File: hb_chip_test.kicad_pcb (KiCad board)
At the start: 2 copper layers, 140 parts, among them J1 31-5431-2010_CID2.5.196, J2 31-5431-2010_CID2.5.196, J3 31-5431-2010_CID2.5.196, J4 1945193_12P_CID2.2.928, J5 31-5431-2010_CID2.5.196, J6 31-5431-2010_CID2.5.196, U1 L7812ABD2T-TR_CID8.52.934, U2 MC7912ACD2TR4G_CID8.52.429, U3 LP2981IM5-5.0-NOPB_CID8.52.176, U5 TL084, U6 MCP3202, U7 REF5050ID

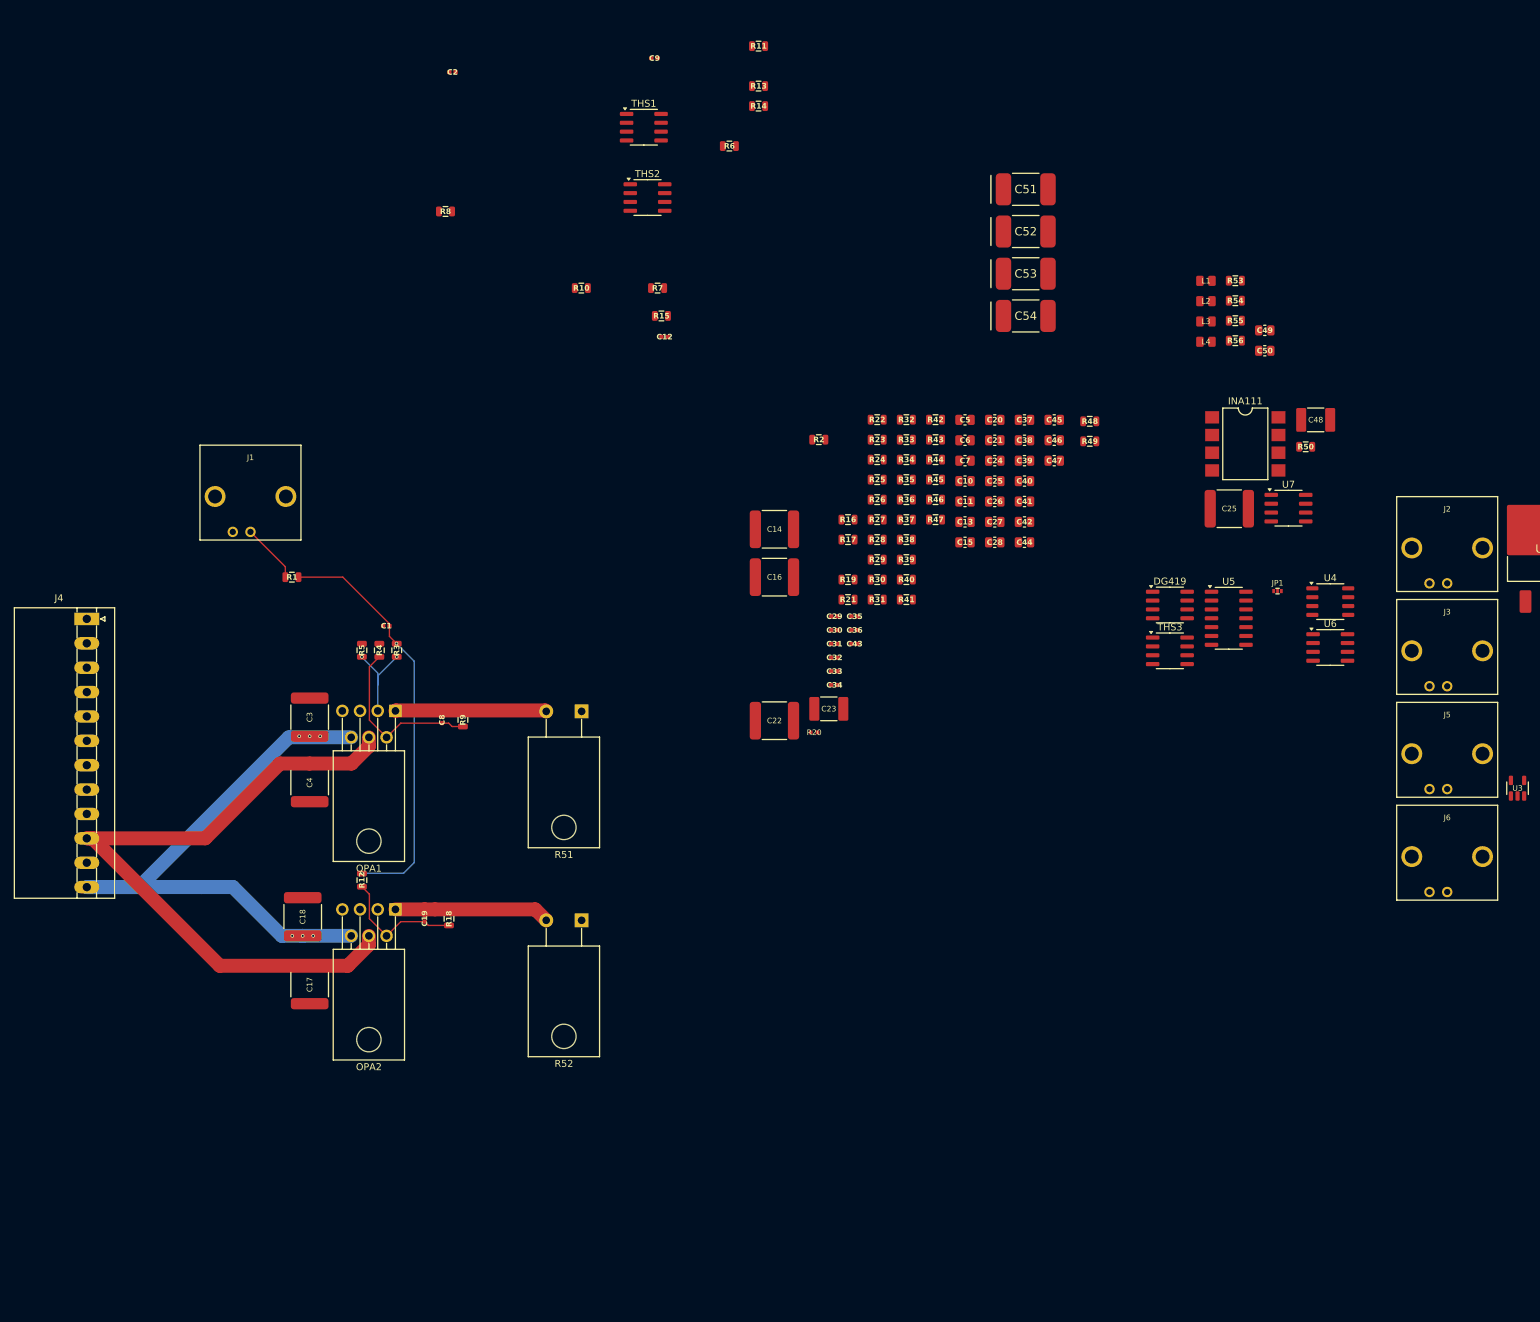
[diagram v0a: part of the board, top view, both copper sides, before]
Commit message: Variable amps and offset circuit
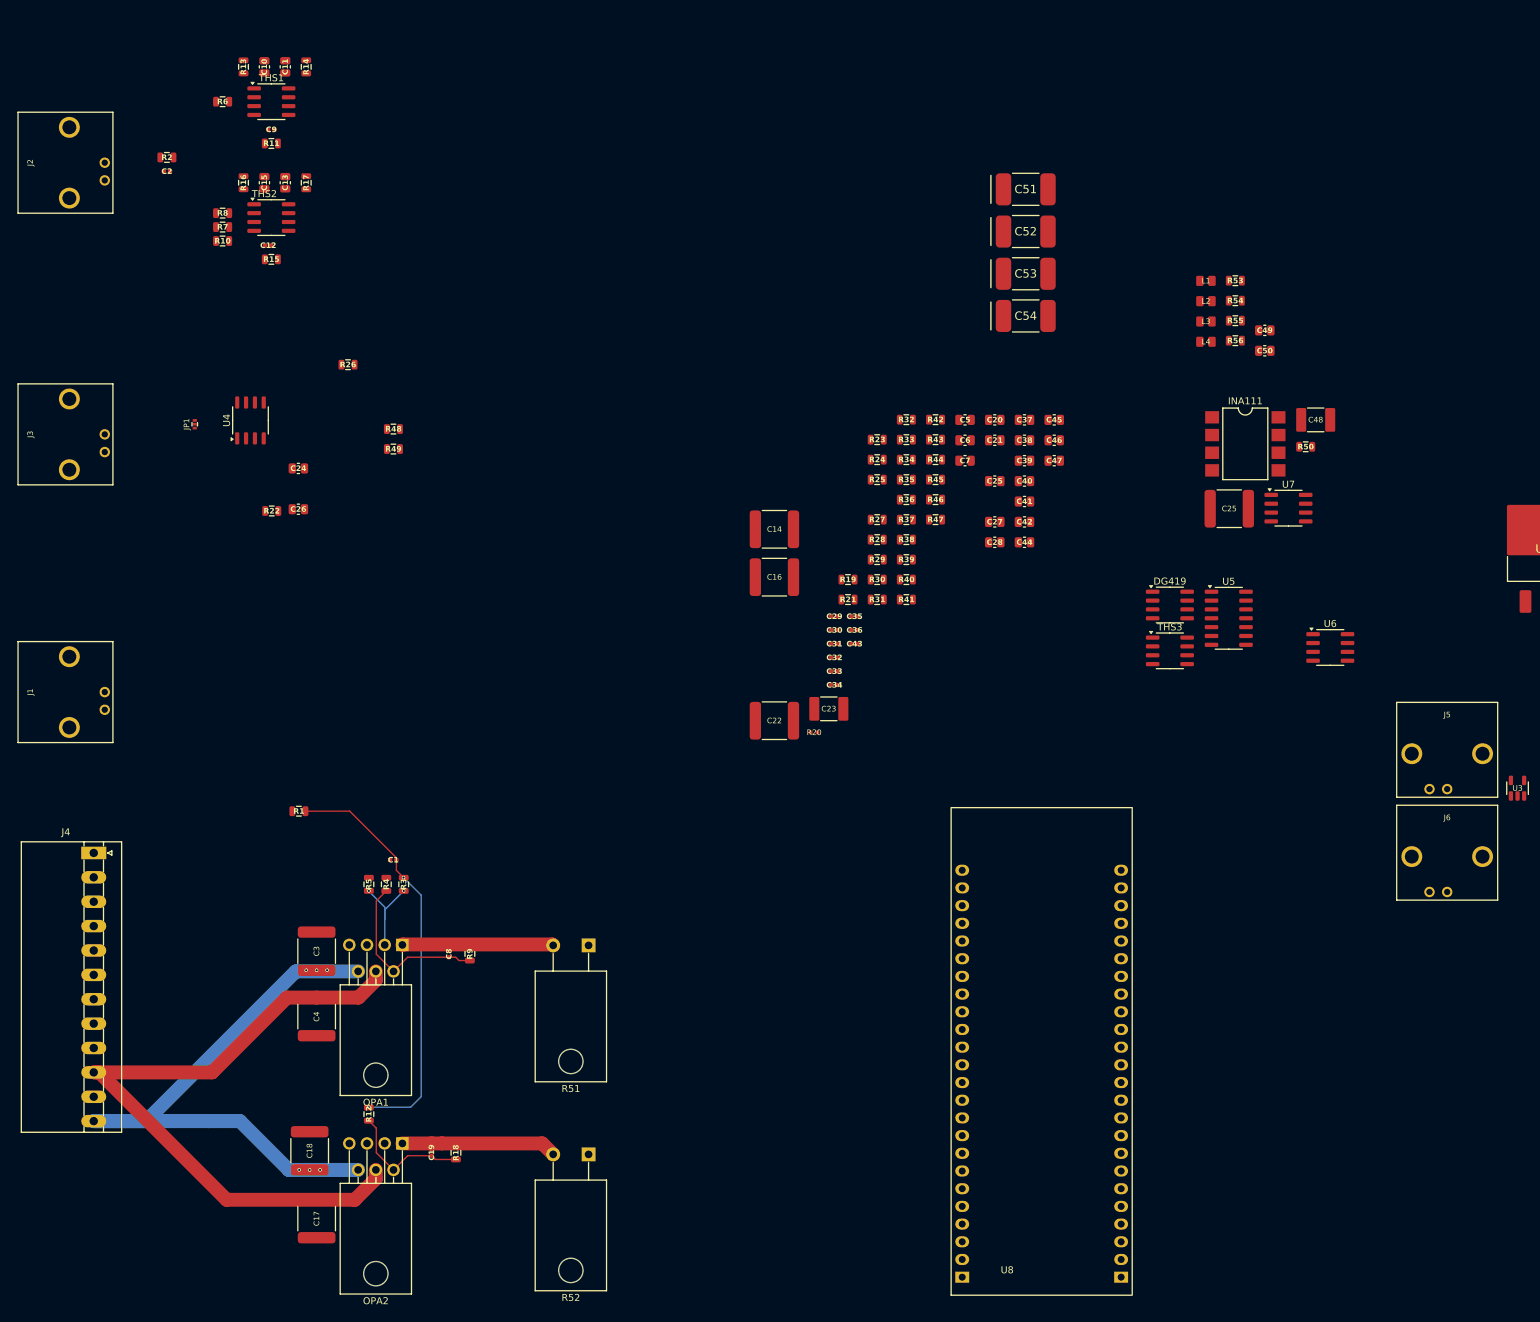
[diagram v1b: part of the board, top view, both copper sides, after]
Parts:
- added U8: Tang_Nano_9K, 0my_project:DIP-48_TangNano9K, F.Cu at (160.6, 163.8)
- moved J2 205.4 mm to (21.0, 33.0), turned to 90 degrees
- moved J3 200.2 mm to (21.0, 72.0), turned to 90 degrees
- moved JP1 157.3 mm to (39.0, 70.5), turned to 90 degrees
- moved U4 157.2 mm to (47.0, 70.0), turned to 90 degrees
- moved C10 116.9 mm to (49.0, 19.2), turned to 90 degrees
- moved C11 115.8 mm to (52.0, 19.2), turned to 90 degrees
- moved C15 113.1 mm to (49.0, 35.9), turned to 90 degrees
- moved C13 109.1 mm to (52.0, 35.9), turned to 90 degrees
- moved R2 102.0 mm to (35.0, 32.2)
- moved C24 100.0 mm to (53.9, 76.9)
- moved C26 100.0 mm to (53.9, 82.8)
- moved R48 100.0 mm to (67.5, 71.2)
- moved R49 100.0 mm to (67.5, 74.1)
- moved R16 99.4 mm to (46.0, 35.9), turned to 90 degrees
- moved R17 93.1 mm to (55.0, 35.9), turned to -90 degrees
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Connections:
- R8 pad 1: unconnected-(R8-Pad1) -> GND
- R8 pad 2: unconnected-(R8-Pad2) -> Net-(THS2--)
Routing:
- net Net-(J1-Pad1): track 8.57 -> 0.00 mm

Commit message: HB driver jumpers + PCBv1
TangNano9k has been wired.

Jumpers place for the hb drive but no bnc's for this. If something else is to drive it it can be done from jumpers.

PCB is in the layout v1 now. Still missing socket for the chip.
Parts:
- removed the C25 at (153.9, 78.7)
- added C55: C_0805_100nF_16V_X7R_CID1.2.3078, dtuspace_ipc:C0805_CAPC200X125X130L45N, F.Cu at (211.3, 60.2)
- added C56: C_0805_100nF_16V_X7R_CID1.2.3078, dtuspace_ipc:C0805_CAPC200X125X130L45N, F.Cu at (219.0, 68.3)
- added C57: C_0402_3.3nF_16V_X7R_CID1.2.2599, dtuspace_ipc:C0402_CAPC100X50X61L25N, F.Cu at (112.4, 66.3)
- added C58: C_2917_47uF_20V_20%_CID1.3.892, dtuspace_ipc:C2917_CAPC730X430X310L130N, F.Cu at (101.3, 157.0)
- added C59: C_2917_47uF_20V_20%_CID1.3.892, dtuspace_ipc:C2917_CAPC730X430X310L130N, F.Cu at (112.0, 157.0)
- added C60: C_2917_47uF_20V_20%_CID1.3.892, dtuspace_ipc:C2917_CAPC730X430X310L130N, F.Cu at (129.8, 157.0)
- added C61: C_2917_47uF_20V_20%_CID1.3.892, dtuspace_ipc:C2917_CAPC730X430X310L130N, F.Cu at (141.0, 157.0)
- added D1: CUS520,H3F_CID4.2.447, dtuspace_ipc:SOD250X130X120L30X30N, F.Cu at (235.5, 108.0)
- added D2: CUS520,H3F_CID4.2.447, dtuspace_ipc:SOD250X130X120L30X30N, F.Cu at (235.5, 104.0)
- added J13: 2x8, dtuspace_ipc:HEADER-P254-2x8, F.Cu at (225.5, 120.0)
- added J7: 31-5431-2010_CID2.5.196, dtuspace_ipc:AMPHENOL_31-5431-2010, F.Cu at (240.9, 65.8)
- added J8: 2x8, dtuspace_ipc:HEADER-P254-2x8, F.Cu at (212.8, 154.8)
- added JP2: Jumper_3_Open, dtuspace_ipc:HEADER-P254-1x3, F.Cu at (178.9, 33.1)
- added JP3: Jumper_3_Open, dtuspace_ipc:HEADER-P254-1x3, F.Cu at (214.0, 72.3)
- added JP4: Jumper_3_Open, dtuspace_ipc:HEADER-P254-1x3, F.Cu at (187.9, 51.1)
- added JP5: Jumper_3_Open, dtuspace_ipc:HEADER-P254-1x3, F.Cu at (114.5, 48.9)
- added JP6: Jumper_3_Open, dtuspace_ipc:HEADER-P254-1x3, F.Cu at (114.4, 35.2)
- added L5: L_3.3uH_870mA_CID7.3.944, dtuspace_ipc:L0805_INDC200X125X140L50N, F.Cu at (104.7, 162.5)
- added L6: L_3.3uH_870mA_CID7.3.944, dtuspace_ipc:L0805_INDC200X125X140L50N, F.Cu at (108.7, 162.5)
- added L7: L_3.3uH_870mA_CID7.3.944, dtuspace_ipc:L0805_INDC200X125X140L50N, F.Cu at (133.0, 161.0)
- added L8: L_3.3uH_870mA_CID7.3.944, dtuspace_ipc:L0805_INDC200X125X140L50N, F.Cu at (137.5, 163.5)
- added R57: R_0805_51R1_CID10.9.208, dtuspace_ipc:R0805_RESC200X125X50L35N, F.Cu at (176.4, 29.6)
- added R58: R_0805_511k_CID10.9.489, dtuspace_ipc:R0805_RESC200X125X50L35N, F.Cu at (217.4, 57.4)
- added R59: R_0805_511k_CID10.9.489, dtuspace_ipc:R0805_RESC200X125X50L35N, F.Cu at (215.4, 57.4)
- added R60: R_0805_511k_CID10.9.489, dtuspace_ipc:R0805_RESC200X125X50L35N, F.Cu at (214.9, 68.2)
- added R61: R_0805_1M21_CID10.9.5950, dtuspace_ipc:R0805_RESC200X125X50L35N, F.Cu at (212.9, 68.3)
- added R62: R_0805_10R0_CID10.9.4757, dtuspace_ipc:R0805_RESC200X125X50L35N, F.Cu at (211.3, 58.2)
- added R63: R_0805_51k1_CID10.9.5890, dtuspace_ipc:R0805_RESC200X125X50L35N, F.Cu at (208.9, 68.3)
- added R64: R_0805_5k11_CID10.9.467, dtuspace_ipc:R0805_RESC200X125X50L35N, F.Cu at (210.9, 68.3)
- added R65: R_0805_10R0_CID10.9.4757, dtuspace_ipc:R0805_RESC200X125X50L35N, F.Cu at (217.0, 68.2)
- added R66: R_0805_9k53_CID10.9.5867, dtuspace_ipc:R0805_RESC200X125X50L35N, F.Cu at (227.4, 113.5)
- added R67: R_0805_5k11_CID10.9.467, dtuspace_ipc:R0805_RESC200X125X50L35N, F.Cu at (229.4, 113.5)
- added R68: R_0805_1K_CID10.99.611, dtuspace_ipc:R0805_RESC200X125X50L35N, F.Cu at (111.9, 64.8)
- added U9: TL082, dtuspace_ipc:SOIC8P127_490X600X175L83X41N, F.Cu at (215.8, 62.7)
- C39, C46, C47: value C_0805_100nF_16V_X7R_CID1.2.3078 -> C_0402_22nF_16V_X7R_CID1.2.2613; footprint dtuspace_ipc:C0805_CAPC200X125X130L45N -> dtuspace_ipc:C0402_CAPC100X50X61L25N
- JP1: footprint dtuspace_ipc:2_WAY_SOLDER_JUMPER -> dtuspace_ipc:HEADER-P254-1x3
- R35, R46: value R_0805_11k0_CID10.9.5869 -> R_0805_26k1_CID10.9.5881
- R38, R41, R43, R45: value R_0805_11k0_CID10.9.5869 -> R_0805_11k5_CID10.9.5870
- R40, R44: value R_0805_5k62_CID10.9.159 -> R_0805_11k5_CID10.9.5870
- R47: value R_0805_5k62_CID10.9.159 -> R_0805_26k1_CID10.9.5881
- R53: value R_0805_220R_CID10.9.602 -> R_0805_1K_CID10.99.611
- R55: value R_0805_2M49_CID10.9.5964 -> R_0805_2k49_CID10.9.5859
- R56: value R_0805_10M0_CID10.9.5993 -> R_0805_10k0_CID10.9.476
- moved LD_SML-P11VTT86R2 223.8 mm to (71.0, 138.5), turned to 90 degrees
- moved LD_SML-P11VTT86R3 213.9 mm to (71.0, 118.0), turned to 180 degrees
- moved LD_SML-P11VTT86R1 211.4 mm to (71.0, 107.9), turned to 90 degrees
- moved U2 173.8 mm to (74.8, 127.6), turned to 180 degrees
- moved U1 168.4 mm to (74.8, 148.6), turned to 180 degrees
- moved U3 155.7 mm to (73.9, 107.9), turned to 90 degrees
- moved LD_SML-P11VTT86R4 143.9 mm to (164.2, 134.8), turned to 90 degrees
- moved L3 130.4 mm to (90.0, 146.0), turned to 90 degrees
- moved C53 124.5 mm to (83.5, 148.5), turned to -90 degrees
- moved L4 117.7 mm to (90.4, 129.8), turned to -90 degrees
- moved C20 114.7 mm to (68.0, 146.0), turned to -90 degrees
- moved L2 113.1 mm to (85.9, 108.9), turned to 180 degrees
- moved C43 112.5 mm to (225.5, 37.0), turned to 90 degrees
- moved C51 109.4 mm to (171.0, 145.5)
- moved C54 104.1 mm to (83.4, 127.3), turned to -90 degrees
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- renumbered OPA1 to U10, THS1 to U11, THS2 to U12, OPA2 to U13, INA111 to U15, DG419 to U16, THS3 to U17
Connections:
- C17 pad 1: +10V -> Net-(U13-V+)
- C18 pad 1: -10V -> Net-(U13-V-)
- C22 pad 2: +5VA -> +5V
- C3 pad 1: -10V -> Net-(U10-V-)
- C36 pad 2: Net-(THS3-Out) -> Net-(U17-Out)
- C39 pad 1: GND -> Net-(U5A--)
- C4 pad 1: +10V -> Net-(U10-V+)
- C42 pad 1: Net-(U5A--) -> Net-(C42-Pad1)
- C42 pad 2: Net-(C42-Pad2) -> GND
- C44 pad 1: GND -> Net-(C44-Pad1)
- C44 pad 2: Net-(C44-Pad2) -> GND
- C45 pad 1: Net-(U5B--) -> Net-(C45-Pad1)
- C45 pad 2: Net-(C45-Pad2) -> GND
- C46 pad 1: GND -> Net-(U5B--)
- C47 pad 2: Net-(C47-Pad2) -> Net-(JP3-C)
- C8 pad 1: Net-(OPA1--) -> GND
- J3 pad 1: Net-(JP1-C) -> Net-(J3-Pad1)
- J5 pad 1: Net-(C47-Pad2) -> Net-(JP3-C)
- JP1 pad 3: Net-(DG419-IN) -> Net-(JP1-B)
- R20 pad 1: Net-(INA111-R_G-Pad8) -> Net-(R20-Pad1)
- R20 pad 2: Net-(INA111-R_G-Pad1) -> Net-(JP2-A)
- R26 pad 1: Net-(DG419-IN) -> Net-(JP1-B)
- R34 pad 2: Net-(THS3-Out) -> Net-(U17-Out)
- R35 pad 1: Net-(THS3-Out) -> Net-(U5A--)
- R38 pad 1: Net-(C39-Pad2) -> Net-(U17-Out)
- R38 pad 2: Net-(U5A--) -> Net-(C45-Pad1)
- R39 pad 1: Net-(THS3-Out) -> Net-(U17-Out)
- R4 pad 2: Net-(OPA1--) -> Net-(U10--)
- R40 pad 1: Net-(U5A--) -> Net-(C45-Pad1)
- R40 pad 2: Net-(C42-Pad2) -> Net-(U5A--)
- R41 pad 1: Net-(C42-Pad2) -> Net-(C39-Pad2)
- R41 pad 2: Net-(C44-Pad2) -> Net-(C42-Pad1)
- R43 pad 1: Net-(C44-Pad2) -> Net-(C42-Pad1)
- R44 pad 1: Net-(U5B--) -> Net-(C46-Pad2)
- R44 pad 2: Net-(C45-Pad2) -> Net-(C44-Pad1)
- R45 pad 1: Net-(C45-Pad2) -> Net-(C44-Pad1)
- R45 pad 2: Net-(C46-Pad2) -> Net-(U5C--)
- R46 pad 1: Net-(C46-Pad2) -> Net-(U5B--)
- R46 pad 2: Net-(U5C--) -> Net-(C46-Pad2)
- R47 pad 2: Net-(C47-Pad2) -> Net-(JP3-C)
- R53 pad 1: Net-(U6-CH0) -> Net-(J7-Pad1)
- R53 pad 2: Net-(C47-Pad2) -> Net-(D1-PadA)
- R54 pad 1: Net-(U6-CH1) -> Net-(U6-CH0)
- R54 pad 2: Net-(R54-Pad2) -> Net-(D1-PadA)
- R55 pad 1: Net-(R54-Pad2) -> Net-(U6-CH1)
- R56 pad 2: Net-(R54-Pad2) -> Net-(U6-CH1)
- R9 pad 1: Net-(OPA1--) -> GND
- U10 pad 2: Net-(OPA1--) -> Net-(U10--)
- U10 pad 4: +10V -> Net-(U10-V+)
- U10 pad 6: -10V -> Net-(U10-V-)
- U13 pad 4: +10V -> Net-(U13-V+)
- U13 pad 6: -10V -> Net-(U13-V-)
- U15 pad 1: Net-(INA111-R_G-Pad1) -> Net-(R20-Pad1)
- U15 pad 8: Net-(INA111-R_G-Pad8) -> Net-(JP2-C)
- U16 pad 6: Net-(DG419-IN) -> Net-(JP4-C)
- U17 pad 6: Net-(THS3-Out) -> Net-(U17-Out)
- U2 pad 1: Net-(U2-VIN) -> GND
- U2 pad 3: GND -> Net-(U2-VIN)
- U4 pad 7: Net-(DG419-IN) -> Net-(JP1-B)
- U5 pad 1: Net-(C42-Pad2) -> Net-(C39-Pad2)
- U5 pad 7: Net-(C45-Pad2) -> Net-(C46-Pad2)
- U5 pad 8: Net-(C47-Pad2) -> Net-(JP3-C)
- U6 pad 1: unconnected-(U6-~{CS}/SHDN-Pad1) -> Net-(U6-~{CS}/SHDN)
- U6 pad 5: unconnected-(U6-DIN-Pad5) -> Net-(U6-DIN)
- U6 pad 6: unconnected-(U6-DOUT-Pad6) -> Net-(U6-DOUT)
- U6 pad 7: unconnected-(U6-CLK-Pad7) -> Net-(U6-CLK)
- U8 pad 10: unconnected-(U8-30_IOB13B-Pad10) -> Net-(U8-30_IOB13B)
- U8 pad 11: unconnected-(U8-33_IOB23A-Pad11) -> Net-(U8-33_IOB23A)
- U8 pad 12: unconnected-(U8-34_IOB23B-Pad12) -> Net-(U8-34_IOB23B)
- U8 pad 32: unconnected-(U8-70_IOT41B-Pad32) -> Net-(U8-70_IOT41B)
- U8 pad 33: unconnected-(U8-71_IOT41A-Pad33) -> Net-(U8-71_IOT41A)
- U8 pad 34: unconnected-(U8-72_IOT39B-Pad34) -> Net-(U8-72_IOT39B)
- U8 pad 35: unconnected-(U8-73_IOT39A-Pad35) -> Net-(U8-73_IOT39A)
- U8 pad 36: unconnected-(U8-74_IOT38B-Pad36) -> Net-(U8-74_IOT38B)
- U8 pad 37: unconnected-(U8-75_IOT38A-Pad37) -> Net-(U8-75_IOT38A)
- U8 pad 38: unconnected-(U8-76_IOT37B-Pad38) -> Net-(U8-76_IOT37B)
- U8 pad 39: unconnected-(U8-77_IOT37A-Pad39) -> Net-(U8-77_IOT37A)
- U8 pad 5: unconnected-(U8-25_IOB8A-Pad5) -> Net-(U8-25_IOB8A)
- U8 pad 6: unconnected-(U8-26_IOB8B-Pad6) -> Net-(U8-26_IOB8B)
- U8 pad 7: unconnected-(U8-27_IOB11A-Pad7) -> Net-(U8-27_IOB11A)
- U8 pad 8: unconnected-(U8-28_IOB11B-Pad8) -> Net-(U8-28_IOB11B)
- U8 pad 9: unconnected-(U8-29_IOB13A-Pad9) -> Net-(U8-29_IOB13A)
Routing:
- net +12V: track 0.00 -> 375.0 mm, vias 0 -> 8
- net -12V: track 0.00 -> 262.6 mm, vias 0 -> 5
- net +15V: track 0.00 -> 206.4 mm, vias 0 -> 5
- net +5V: track 0.00 -> 203.2 mm, vias 0 -> 2
- net Net-(U6-VDD/VREF): track 0.00 -> 83.8 mm
- net Net-(J7-Pad1): track 0.00 -> 67.0 mm, vias 0 -> 1
- net Net-(J1-Pad1): track 0.00 -> 66.1 mm, vias 0 -> 1
- net +10V: track 97.9 -> 35.9 mm
- net Net-(U17-Out): track 0.00 -> 51.2 mm
- net -15V: track 0.00 -> 46.3 mm
- net Net-(JP3-C): track 0.00 -> 45.8 mm, vias 0 -> 1
- net -10V: track 87.7 -> 45.1 mm, vias 6 -> 4
- net Net-(J3-Pad1): track 0.00 -> 35.7 mm
- net Net-(OPA1--): track 25.2 -> 0.00 mm
- net Net-(R58-Pad2): track 0.00 -> 25.1 mm
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- added copper zone on B.Cu, net GND
- added copper zone on F.Cu, net GND
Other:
- board text added: "Husk Sense-pins over alt! (eg R51/52)"
